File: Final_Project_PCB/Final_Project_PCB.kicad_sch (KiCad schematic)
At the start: 17 parts, among them J1 Screw_Terminal_01x03, J2 SR04 Sensor Jarak, J3 LDR, J4 Soil Moisture Sensor, K1 SRD-05VDC-SL-C, Q1 BC547, U1 ESP32-DEVKIT-V1, U2 DHT11

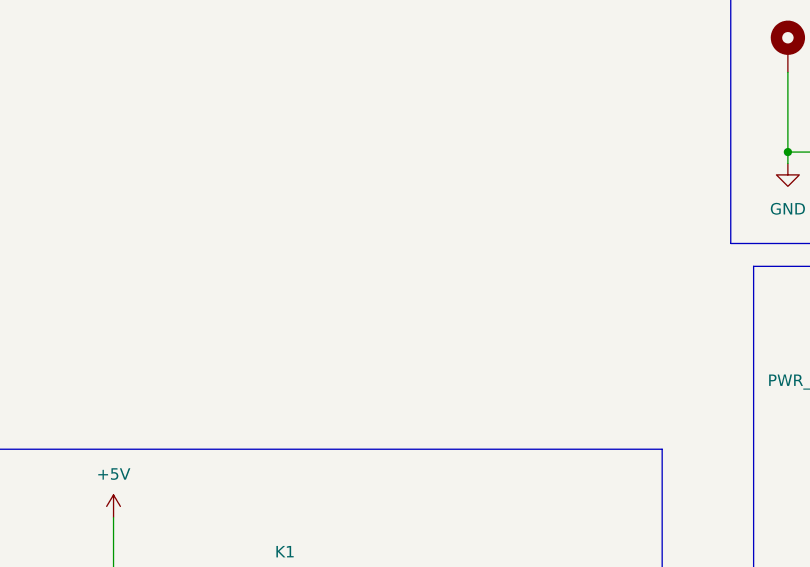
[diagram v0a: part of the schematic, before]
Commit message: Adding Barrel Jack for 5v Source
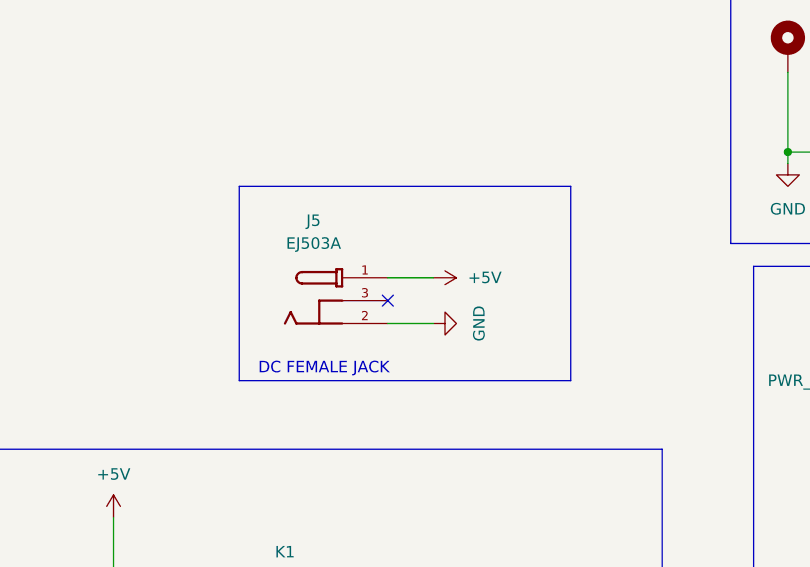
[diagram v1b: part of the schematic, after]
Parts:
- added J5: EJ503A, BARREL JACK 2.1MM KICAD:MPD_EJ503A, symbol EJ503A:EJ503A
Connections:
- net +5V: now also J5.1
- net GND: now also J5.2
- no-connect marks 19 -> 20
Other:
- note added: "DC FEMALE JACK"
